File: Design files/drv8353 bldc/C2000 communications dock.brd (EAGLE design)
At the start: 55.9 x 53 mm, 28 parts, among them IC1 ADUM1311ARWZ, J3 SS-6488-NF-A431, U1 3352T-1-203LF

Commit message: adds enable link to comm board
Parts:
- removed LED1, LED2: (no value), eagle-ltspice:LED_SML0603
- removed R1, R2: 50, rcl:R0603
- added J1: B03B-HCMKS, AUX Lib:B03BHCMKS
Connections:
- removed net N$17: LED1.C, R1.2
- removed net N$18: LED2.C, R2.2
- removed net N$3: LED2.A, U$1.39
- new net N$1: J1.1, U$1.40
- net GND: now also J1.3; no longer R1.1, R2.1
- net N$2: now also J1.2, U$1.39; no longer LED1.A, U$1.40
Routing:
- net GND: track 37.5 -> 52.0 mm, vias 20 -> 18
- net N$2: track 3.06 -> 16.5 mm
- net N$1: track 0.00 -> 10.1 mm
- net N$3: track 3.06 -> 0.00 mm
- net N$18: track 2.21 -> 0.00 mm
- net N$17: track 2.21 -> 0.00 mm

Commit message: adds chip select to com board
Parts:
- removed SV2: (no value), con-lsta:FE05-1
- added SV3: (no value), con-lsta:FE06
- IC1: value ADUM1311ARWZ -> ADUM1411ARWZ
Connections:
- removed net 5V: SV1.2, U$1.21
- new net CS: IC1.12, SV1.2, U$1.13
- new net ECS: IC1.5, J3.6, SV3.5
- net ECLK: now also SV3.4; no longer SV2.4
- net EGND: now also SV3.1; no longer SV2.2
- net EMISO: now also IC1.6, SV3.6; no longer IC1.5, SV2.5
- net EMOSI: now also SV3.3; no longer SV2.3
- net EVD: now also SV3.2; no longer SV2.1
- net MISO: now also IC1.11; no longer IC1.12
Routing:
- net CS: track 0.00 -> 37.9 mm, vias 0 -> 2
- net 5V: track 26.6 -> 0.00 mm
- net ECS: track 0.00 -> 14.7 mm
- net EGND: track 20.6 -> 13.3 mm
- net ECLK: track 13.3 -> 17.9 mm
- net EMOSI: track 20.3 -> 24.7 mm
- net GND: track 52.0 -> 49.4 mm, vias 18 -> 20
- net EVD: track 26.1 -> 27.7 mm
- net MISO: track 37.9 -> 39.3 mm
- net CLK: track 42.1 -> 43.4 mm
- net EMISO: track 13.8 -> 14.6 mm
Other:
- board text added: "CS"
- board text removed: "5V"

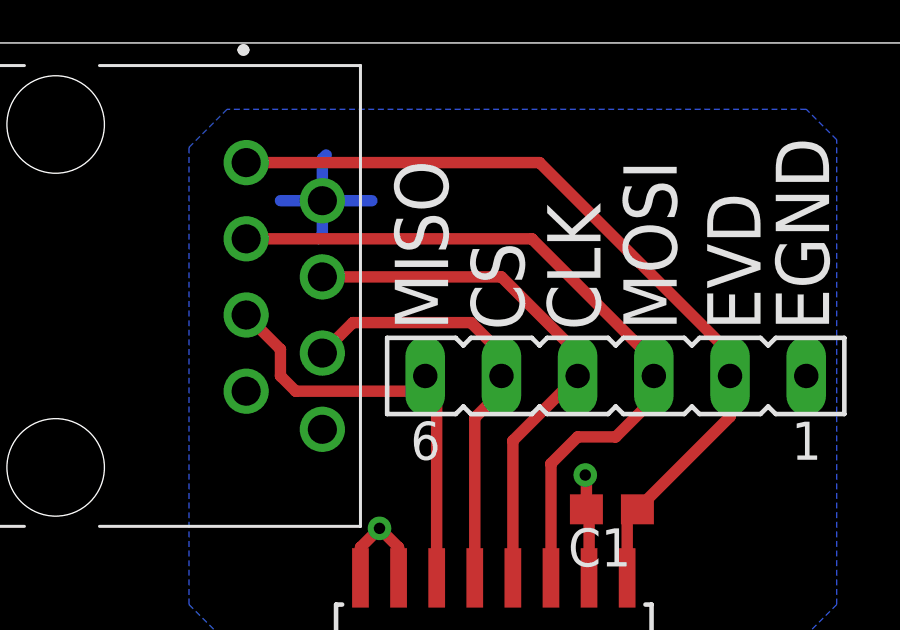
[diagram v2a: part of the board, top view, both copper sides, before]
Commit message: reroute to match aux
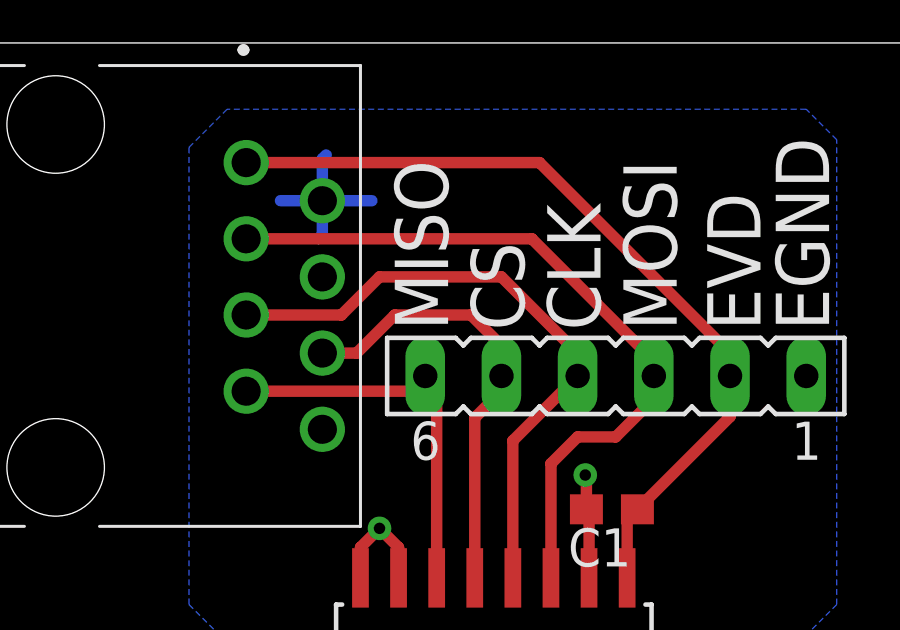
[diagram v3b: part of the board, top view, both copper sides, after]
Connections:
- net ECLK: now also J3.5; no longer J3.4
- net EMISO: now also J3.7; no longer J3.5
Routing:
- net ECLK: track 17.9 -> 21.0 mm
- net EMISO: track 14.6 -> 13.1 mm
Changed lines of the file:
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@@
 <signal name="EVD">
 <contactref element="IC1" pad="1"/>
-<contactref element="J3" pad="1"/>
 <contactref element="C1" pad="1"/>
 <wire x1="29.845" y1="35.179" x2="29.845" y2="37.123" width="0.381" layer="1"/>
@@
 <wire x1="26.924" y1="49.022" x2="33.274" y2="42.672" width="0.381" layer="1"/>
 <wire x1="33.274" y1="42.672" x2="33.274" y2="41.91" width="0.381" layer="1"/>
-<wire x1="17.145" y1="49.022" x2="26.924" y2="49.022" width="0.381" layer="1"/>
 <wire x1="33.274" y1="41.91" x2="33.274" y2="40.552" width="0.381" layer="1"/>
 <wire x1="33.274" y1="40.552" x2="30.187" y2="37.465" width="0.381" layer="1"/>
+<contactref element="J3" pad="1"/>
+<wire x1="17.145" y1="49.022" x2="26.924" y2="49.022" width="0.381" layer="1"/>
 </signal>
 <signal name="ECLK">
 <contactref element="IC1" pad="4"/>
-<contactref element="J3" pad="4"/>
 <contactref element="SV3" pad="4"/>
 <wire x1="26.035" y1="35.179" x2="26.035" y2="39.751" width="0.381" layer="1"/>
 <wire x1="26.035" y1="39.751" x2="28.194" y2="41.91" width="0.381" layer="1"/>
 <wire x1="28.194" y1="41.91" x2="28.194" y2="42.672" width="0.381" layer="1"/>
-<wire x1="28.194" y1="42.672" x2="25.654" y2="45.212" width="0.381" layer="1"/>
-<wire x1="25.654" y1="45.212" x2="19.685" y2="45.212" width="0.381" layer="1"/>
+<wire x1="25.654" y1="45.212" x2="28.194" y2="42.672" width="0.381" layer="1"/>
+<contactref element="J3" pad="5"/>
+<wire x1="21.59" y1="45.212" x2="25.654" y2="45.212" width="0.381" layer="1"/>
+<wire x1="17.145" y1="43.942" x2="20.32" y2="43.942" width="0.381" layer="1"/>
+<wire x1="20.32" y1="43.942" x2="21.59" y2="45.212" width="0.381" layer="1"/>
 </signal>
 <signal name="EMISO">
-<contactref element="J3" pad="5"/>
-<wire x1="18.288" y1="42.799" x2="18.288" y2="41.91" width="0.381" layer="1"/>
-<wire x1="18.288" y1="41.91" x2="18.796" y2="41.402" width="0.381" layer="1"/>
-<wire x1="17.145" y1="43.942" x2="18.288" y2="42.799" width="0.381" layer="1"/>
 <contactref element="IC1" pad="6"/>
 <contactref element="SV3" pad="6"/>
 <wire x1="22.606" y1="41.402" x2="23.114" y2="41.91" width="0.381" layer="1"/>
-<wire x1="18.796" y1="41.402" x2="22.606" y2="41.402" width="0.381" layer="1"/>
 <wire x1="23.114" y1="41.91" x2="23.114" y2="41.402" width="0.381" layer="1"/>
 <wire x1="23.495" y1="41.021" x2="23.495" y2="35.179" width="0.381" layer="1"/>
 <wire x1="23.114" y1="41.402" x2="23.495" y2="41.021" width="0.381" layer="1"/>
+<contactref element="J3" pad="7"/>
+<wire x1="17.145" y1="41.402" x2="22.606" y2="41.402" width="0.381" layer="1"/>
 </signal>
 <signal name="EGND">
@@
 </signal>
 <signal name="EMOSI">
-<contactref element="J3" pad="3"/>
 <contactref element="IC1" pad="3"/>
 <contactref element="SV3" pad="3"/>
 <wire x1="30.734" y1="42.418" x2="30.734" y2="41.91" width="0.381" layer="1"/>
-<wire x1="30.734" y1="42.418" x2="26.67" y2="46.482" width="0.381" layer="1"/>
-<wire x1="17.145" y1="46.482" x2="26.67" y2="46.482" width="0.381" layer="1"/>
+<wire x1="26.67" y1="46.482" x2="30.734" y2="42.418" width="0.381" layer="1"/>
 <wire x1="30.734" y1="41.91" x2="30.734" y2="41.148" width="0.381" layer="1"/>
 <wire x1="30.734" y1="41.148" x2="29.464" y2="39.878" width="0.381" layer="1"/>
@@
 <wire x1="28.194" y1="39.878" x2="27.305" y2="38.989" width="0.381" layer="1"/>
 <wire x1="27.305" y1="38.989" x2="27.305" y2="35.179" width="0.381" layer="1"/>
+<contactref element="J3" pad="3"/>
+<wire x1="17.145" y1="46.482" x2="26.67" y2="46.482" width="0.381" layer="1"/>
 </signal>
 <signal name="N$4">
@@
 <signal name="ECS">
 <contactref element="IC1" pad="5"/>
-<contactref element="J3" pad="6"/>
 <contactref element="SV3" pad="5"/>
-<wire x1="19.685" y1="42.672" x2="20.701" y2="43.688" width="0.381" layer="1"/>
-<wire x1="20.701" y1="43.688" x2="24.638" y2="43.688" width="0.381" layer="1"/>
-<wire x1="24.638" y1="43.688" x2="25.654" y2="42.672" width="0.381" layer="1"/>
-<wire x1="25.654" y1="42.672" x2="25.654" y2="41.91" width="0.381" layer="1"/>
 <wire x1="25.654" y1="41.91" x2="25.654" y2="41.402" width="0.381" layer="1"/>
 <wire x1="24.765" y1="40.513" x2="24.765" y2="35.179" width="0.381" layer="1"/>
 <wire x1="25.654" y1="41.402" x2="24.765" y2="40.513" width="0.381" layer="1"/>
+<wire x1="24.638" y1="43.942" x2="25.654" y2="42.926" width="0.381" layer="1"/>
+<wire x1="25.654" y1="41.91" x2="25.654" y2="42.926" width="0.381" layer="1"/>
+<contactref element="J3" pad="6"/>
+<wire x1="24.638" y1="43.942" x2="22.098" y2="43.942" width="0.381" layer="1"/>
+<wire x1="20.828" y1="42.672" x2="19.685" y2="42.672" width="0.381" layer="1"/>
+<wire x1="22.098" y1="43.942" x2="20.828" y2="42.672" width="0.381" layer="1"/>
 </signal>
 <signal name="CS">
